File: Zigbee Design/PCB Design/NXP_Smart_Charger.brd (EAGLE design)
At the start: 108.3 x 63.3 mm, 92 parts, among them IC1 MID400, IC2 MID400, IC3 LMV358, IC4 LMV358, Q1 2222A, Q2 2222A

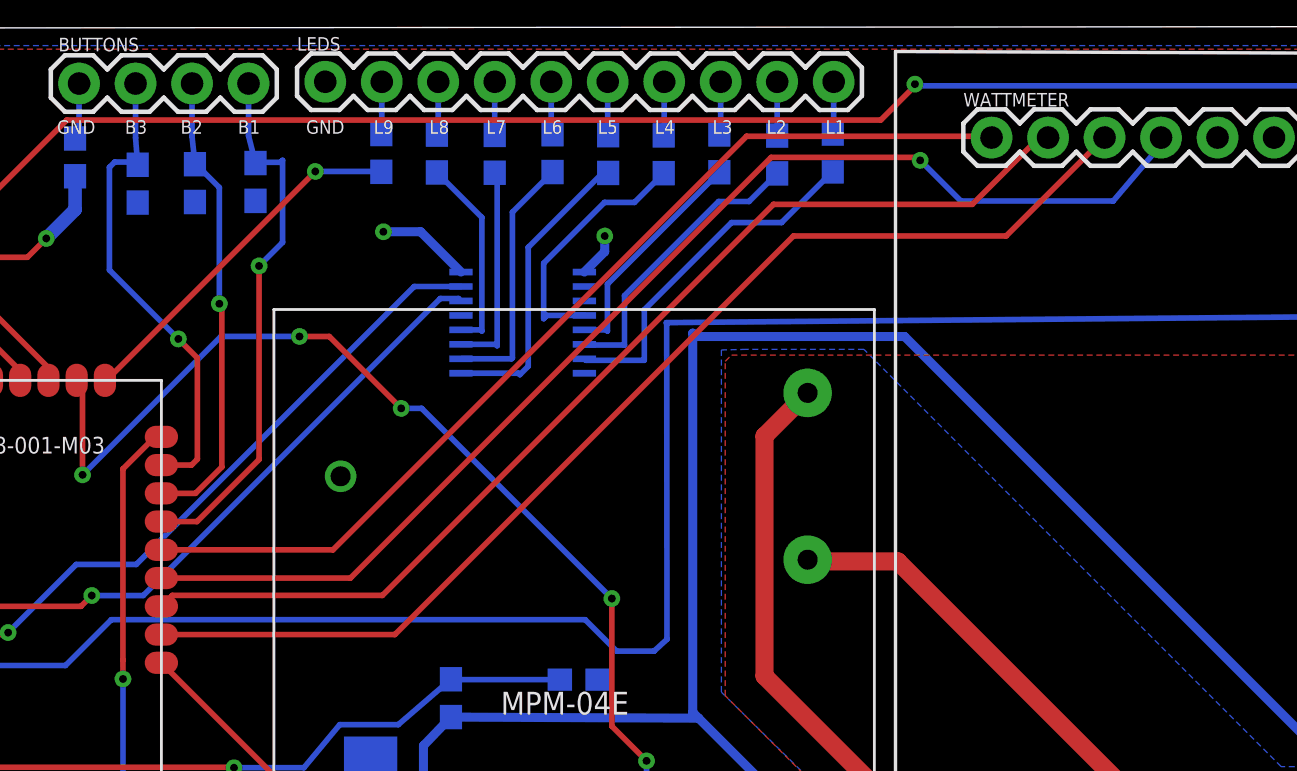
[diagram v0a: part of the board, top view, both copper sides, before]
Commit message: removed io expander
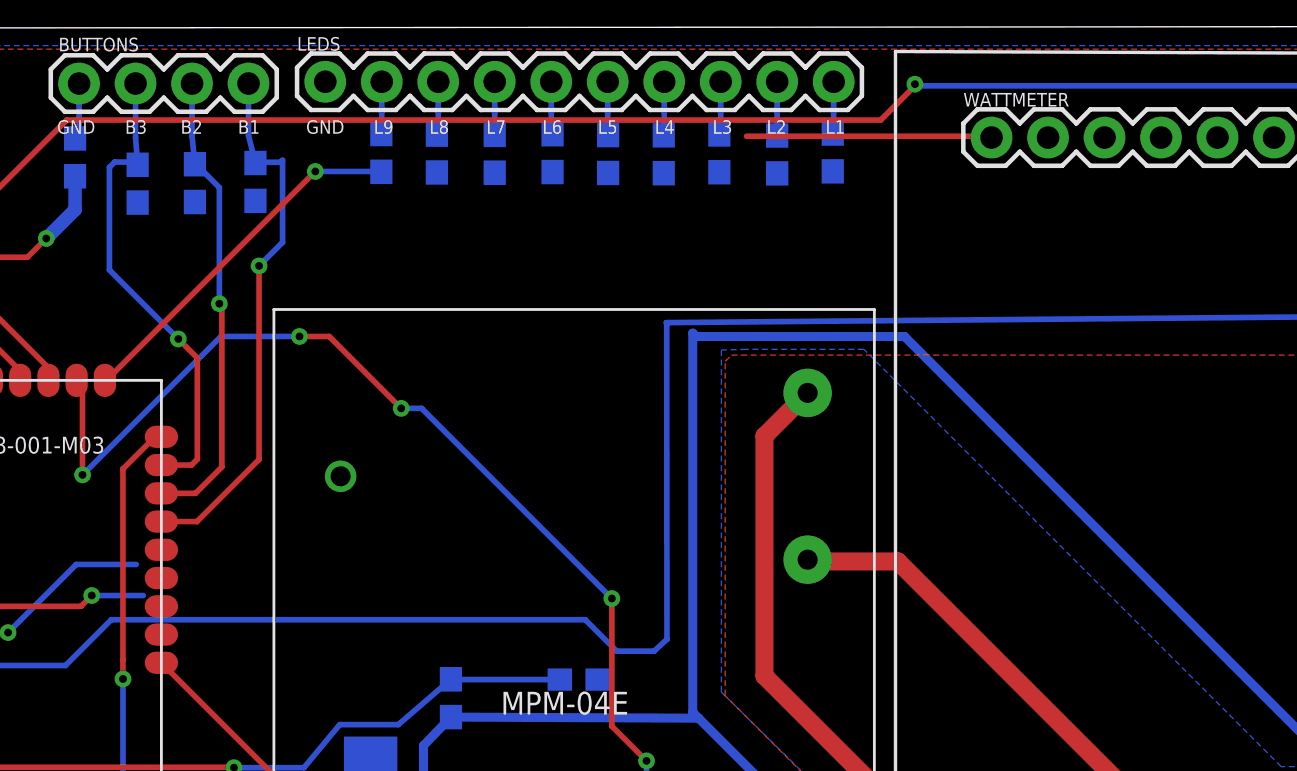
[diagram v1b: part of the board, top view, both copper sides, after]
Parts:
- removed U1: (no value), Smart_Charger:PW
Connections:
- removed net N$39: U1.2
- removed net N$40: U1.3
- net 3.3V: no longer U1.1, U1.16
- net CLK: no longer U1.14
- net GND: no longer U1.8
- net L1: no longer U1.7
- net L2: no longer U1.6
- net L3: no longer U1.5
- net L4: no longer U1.4
- net L5: no longer U1.9
- net L6: no longer U1.10
- net L7: no longer U1.11
- net L8: no longer U1.12
- net SDA: no longer U1.15
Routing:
- net MOSI: track 55.1 -> 0.00 mm, vias 1 -> 0
- net SPI_CLK: track 51.7 -> 0.00 mm
- net MISO: track 48.6 -> 0.00 mm
- net SS: track 45.1 -> 11.0 mm
- net CLK: track 35.2 -> 15.4 mm
- net SDA: track 36.0 -> 16.2 mm
- net L1: track 16.0 -> 0.00 mm
- net L5: track 13.5 -> 0.00 mm
- net L2: track 13.2 -> 0.00 mm
- net L4: track 11.5 -> 0.00 mm
- net L6: track 11.4 -> 0.00 mm
- net L3: track 10.5 -> 0.17 mm
- net L7: track 9.48 -> 0.16 mm
- net L8: track 8.93 -> 0.00 mm
- net 3.3V: track 50.6 -> 44.4 mm, vias 6 -> 4

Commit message: NXP fixes
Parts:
- removed BUTTONS: (no value), SparkFun-Connectors:1X04
- removed LEDS: (no value), SparkFun-Connectors:1X10
- removed R32: 2.0k, SparkFun-Resistors:0603
- removed R37, R38, R39, R40: 10, SparkFun-Resistors:0603
- removed R42, R43: 75, SparkFun-Resistors:0603
- added J4: (no value), SparkFun-Connectors:1X08
- moved R41 18.5 mm to (42.6, 57.3)
- moved R36 18.3 mm to (45.4, 57.3)
- moved R44 18.2 mm to (48.0, 57.3)
- moved R31 5.27 mm to (40.2, 57.3)
- moved JN5168 3.94 mm to (34.3, 49.5)
- moved R34 3.94 mm to (36.3, 57.1), turned to 0 degrees
- moved R27 1.81 mm to (20.2, 37.0), turned to 0 degrees
- moved R35 1.11 mm to (32.5, 57.5)
- moved R4 0.58 mm to (34.8, 8.54)
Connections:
- removed net CLK: JN5168.P25
- removed net FORCE_START: BUTTONS.1, JN5168.P6, R34.1
- removed net FORCE_STOP: BUTTONS.2, JN5168.P7, R32.1
- removed net L7: R39.2
- removed net L8: R40.2
- removed net N$18: LEDS.7, R37.1
- removed net N$46: JN5168.P15
- removed net N$47: JN5168.P16
- removed net N$50: LEDS.6, R38.1
- removed net N$51: LEDS.5, R42.1
- removed net N$52: LEDS.4, R39.1
- removed net N$54: LEDS.2, R43.1
- removed net N$55: JN5168.P22
- removed net N$56: JN5168.P21
- removed net N$75: LEDS.3, R40.1
- removed net SDA: JN5168.P26
- new net BUTTON1: J4.5, JN5168.P6, R31.1
- new net BUTTON2: J4.4, JN5168.P7, R34.1
- net BUTTON3: no longer BUTTONS.3, R31.1
- net GND: now also J4.1; no longer LEDS.1, R32.2
- net L1: now also JN5168.P26
- net L2: now also JN5168.P25
- net L3: now also JN5168.P22
- net L4: now also JN5168.P21; no longer R37.2
- net L5: now also JN5168.P16; no longer R38.2
- net L6: now also JN5168.P15; no longer R42.2
- net L9: no longer R43.2
- net N$14: now also J4.8; no longer LEDS.10
- net N$15: now also J4.7; no longer LEDS.9
- net N$16: now also J4.6; no longer LEDS.8
- net N$93: now also J4.2; no longer BUTTONS.4
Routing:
- net MOSI: track 0.00 -> 59.4 mm, vias 0 -> 1
- net SPI_CLK: track 0.00 -> 51.8 mm
- net MISO: track 0.00 -> 49.5 mm
- net L1: track 0.00 -> 36.2 mm, vias 0 -> 1
- net SS: track 11.0 -> 45.1 mm
- net L2: track 0.00 -> 33.1 mm, vias 0 -> 1
- net L3: track 0.17 -> 28.8 mm, vias 0 -> 1
- net FORCE_START: track 24.6 -> 0.00 mm, vias 1 -> 0
- net BUTTON3: track 21.8 -> 0.00 mm, vias 1 -> 0
- net FORCE_STOP: track 21.3 -> 0.00 mm, vias 1 -> 0
- net BUTTON1: track 0.00 -> 18.9 mm, vias 0 -> 1
- net BUTTON2: track 0.00 -> 18.4 mm, vias 0 -> 1
- net PP_READ: track 42.7 -> 60.9 mm
- net L9: track 16.3 -> 0.00 mm, vias 1 -> 0
- net SDA: track 16.2 -> 0.00 mm, vias 1 -> 0
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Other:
- board text removed: "B3"
- board text removed: "L1"
- board text removed: "L2"
- board text removed: "L3"
- board text removed: "L4"
- board text removed: "L5"
- board text removed: "L6"
- board text removed: "L7"
- board text removed: "L8"
- board text removed: "L9"

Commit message: changes
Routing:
- net GFCI_INT: track 50.7 -> 102.2 mm, vias 1 -> 5
- net 3.3V: track 29.5 -> 32.0 mm, vias 1 -> 2
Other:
- board text added: "FTDI"
- board text added: "L1"
- board text added: "L2"
- board text added: "L3"
